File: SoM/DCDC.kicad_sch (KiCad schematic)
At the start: 29 parts, among them Q1 BC847, Q2 BC847, U3 74LVC2G53, U4 MPM3833C, U5 MPM3833C

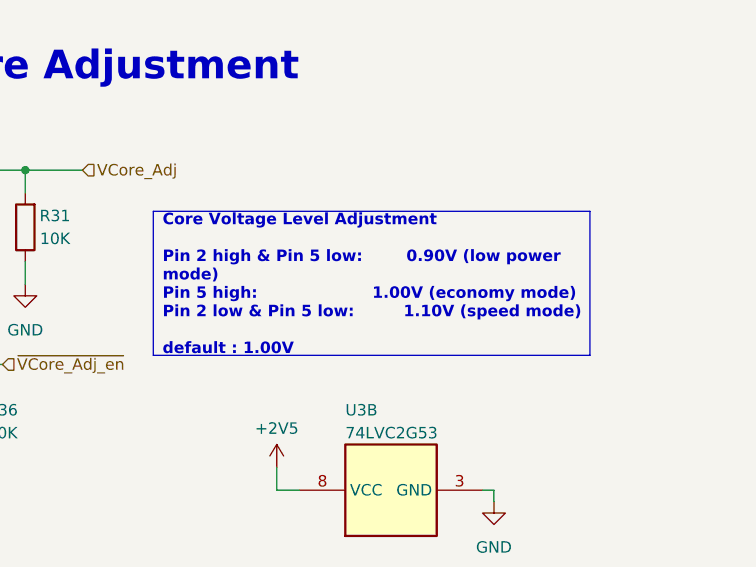
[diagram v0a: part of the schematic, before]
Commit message: Created Version with 0402 components
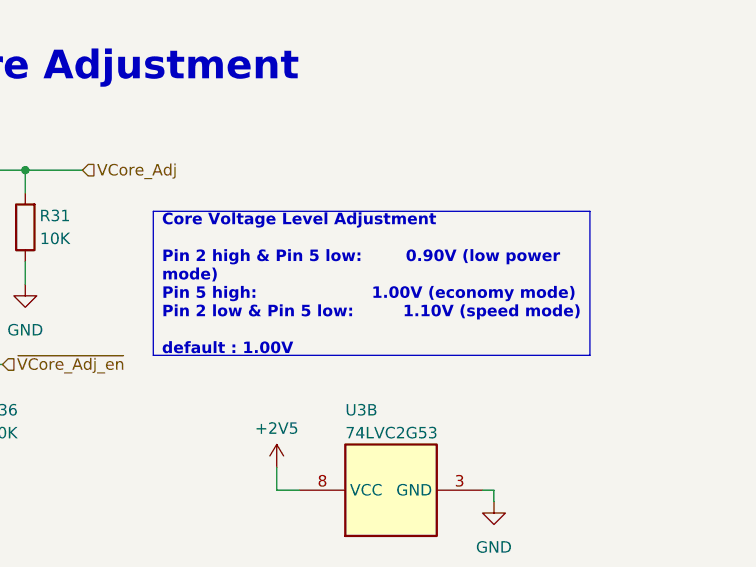
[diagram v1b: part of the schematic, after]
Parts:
- C44, C45, C46, C47: Mouser Part Number 187-CL10A226KQ8NRNE -> GRM188C61C226ME01W; Part Number (none) -> GRM188C61C226ME01W
- D2, D3: Mouser Part Number 710-150060VS75000 -> 150060VS75000; Part Number (none) -> 150060VS75000
- Q1, Q2: Mouser Part Number 637-BC847C-C -> BC847C-C; Part Number (none) -> BC847C-C
- R26, R37: footprint Resistor_SMD:R_0201_0603Metric -> Resistor_SMD:R_0402_1005Metric; Mouser Part Number 71-CRCW02011K00FNED -> MCS04020C1001FE000; Part Number (none) -> MCS04020C1001FE000
- R27, R31, R36, R41: footprint Resistor_SMD:R_0201_0603Metric -> Resistor_SMD:R_0402_1005Metric; Mouser Part Number 71-CRCW0201-10K -> MCS0402MC1002FE000; Part Number (none) -> MCS0402MC1002FE000
- R28: footprint Resistor_SMD:R_0201_0603Metric -> Resistor_SMD:R_0402_1005Metric; Mouser Part Number 71-CRCW0201-20K -> CRCW040220K0FKED; Part Number (none) -> CRCW040220K0FKED
- R29: footprint Resistor_SMD:R_0201_0603Metric -> Resistor_SMD:R_0402_1005Metric; Mouser Part Number 71-CRCW0201100KFNED -> MCS04020C1003FE000; Part Number (none) -> MCS04020C1003FE000
- R30: footprint Resistor_SMD:R_0201_0603Metric -> Resistor_SMD:R_0402_1005Metric; Mouser Part Number 71-CRCW020151K0FKED -> CRCW040251K0FKEDC; Part Number (none) -> CRCW040251K0FKEDC
- R32: footprint Resistor_SMD:R_0201_0603Metric -> Resistor_SMD:R_0402_1005Metric; Mouser Part Number (none) -> MCS04020C2403FE000; Part Number (none) -> MCS04020C2403FE000
- R33: footprint Resistor_SMD:R_0201_0603Metric -> Resistor_SMD:R_0402_1005Metric; Mouser Part Number 71-CRCW020147K0FNED -> CRCW040247K0FKED; Part Number (none) -> CRCW040247K0FKED
- R34: footprint Resistor_SMD:R_0201_0603Metric -> Resistor_SMD:R_0402_1005Metric; Mouser Part Number 71-CRCW0201120KFNED -> MCS04020C1203FE000; Part Number (none) -> MCS04020C1203FE000
- R35: footprint Resistor_SMD:R_0201_0603Metric -> Resistor_SMD:R_0402_1005Metric; Mouser Part Number 71-CRCW020162K0FNED -> CRCW040262K0FKED; Part Number (none) -> CRCW040262K0FKED
- R38: footprint Resistor_SMD:R_0201_0603Metric -> Resistor_SMD:R_0402_1005Metric; Mouser Part Number 71-CRCW0201200KFNED -> CRCW0402200KFKEDC; Part Number (none) -> CRCW0402200KFKEDC
- R39: footprint Resistor_SMD:R_0201_0603Metric -> Resistor_SMD:R_0402_1005Metric; Mouser Part Number 71-CRCW020112K0FNED -> MCS04020C1202FE000; Part Number (none) -> MCS04020C1202FE000
- R40: footprint Resistor_SMD:R_0201_0603Metric -> Resistor_SMD:R_0402_1005Metric; Mouser Part Number 71-CRCW020163K4FNED -> CRCW040263K4FKED; Part Number (none) -> CRCW040263K4FKED
- U3: Mouser Part Number 595-SN74LVC2G53DCUR -> SN74LVC2G53DCUR; Part Number (none) -> SN74LVC2G53DCUR
- U4, U5: Mouser Part Number 946-MPM3833CGRH-Z -> MPM3833CGRH-Z; Part Number (none) -> MPM3833CGRH-Z
